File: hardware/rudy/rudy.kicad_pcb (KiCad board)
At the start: 2 copper layers, 15.7 x 67.1 mm, 23 parts, among them IC1 ATMEGA328-P, P1 CONN1, P2 CONN2, P3 SERPROG, P4 USB_B, U1 LD1117S33TR, Y1 Crystal

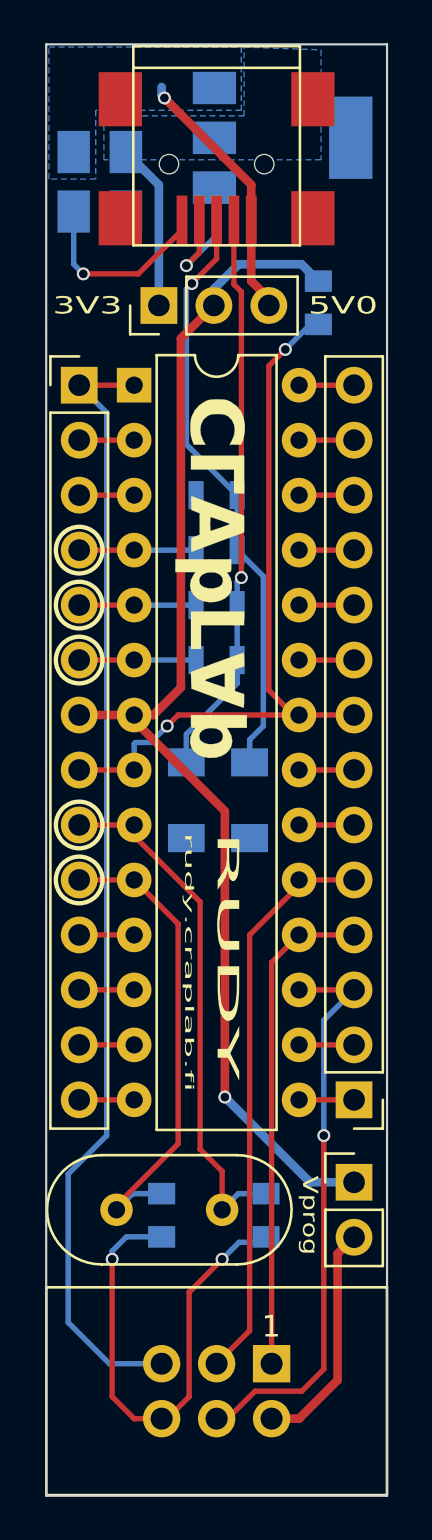
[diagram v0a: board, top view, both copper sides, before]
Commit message: Changed Zener diodes
Changed footprint for D1 and D2 Zener diodes from Mini MILF to SOD-323F
and moved their position in front of R1 and R2.

That came with a bit of rerouting, and trying to keep the pad position
close enough to the initial ones, so I don't have to order new stencils
right away (while even still waiting for them)
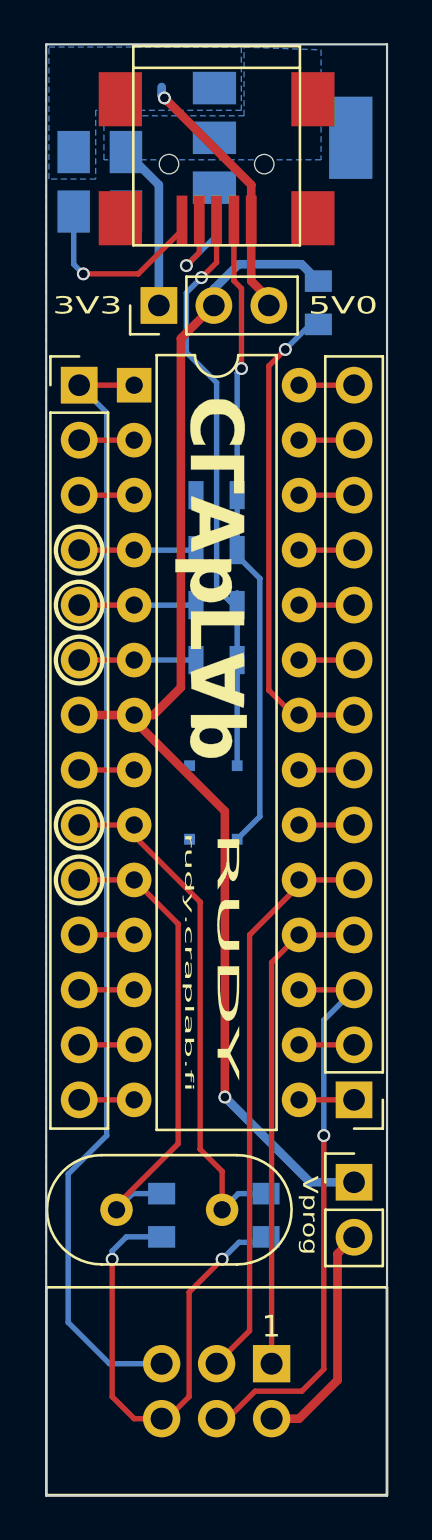
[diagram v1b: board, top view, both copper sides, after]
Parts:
- D1, D2: footprint Diodes_SMD:D_MiniMELF -> Diodes_SMD:D_SOD-323F
- moved D2 2.46 mm to (76.0, 92.1), turned to 180 degrees
- moved D1 2.03 mm to (76.0, 88.7), turned to 180 degrees
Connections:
- P4 pad 2: Net-(D1-Pad1) -> Net-(D2-Pad1)
- P4 pad 3: Net-(D2-Pad1) -> Net-(D1-Pad1)
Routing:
- net GND: track 74.8 -> 65.4 mm, vias 6 -> 5
- net Net-(D2-Pad1): track 27.4 -> 29.7 mm
- net Net-(D1-Pad1): track 26.8 -> 27.4 mm

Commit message: Fixed USB-B component after KiCad update
Turns out 1-3-2-4-5 is a more logical pin arrangement for some people,
and I fucked up paying attention to this, so D+ and D- USB lines got
swapped in the schematic component. Should have been more suspicious
why I had to do so much re-routing after updating the Zener diodes.
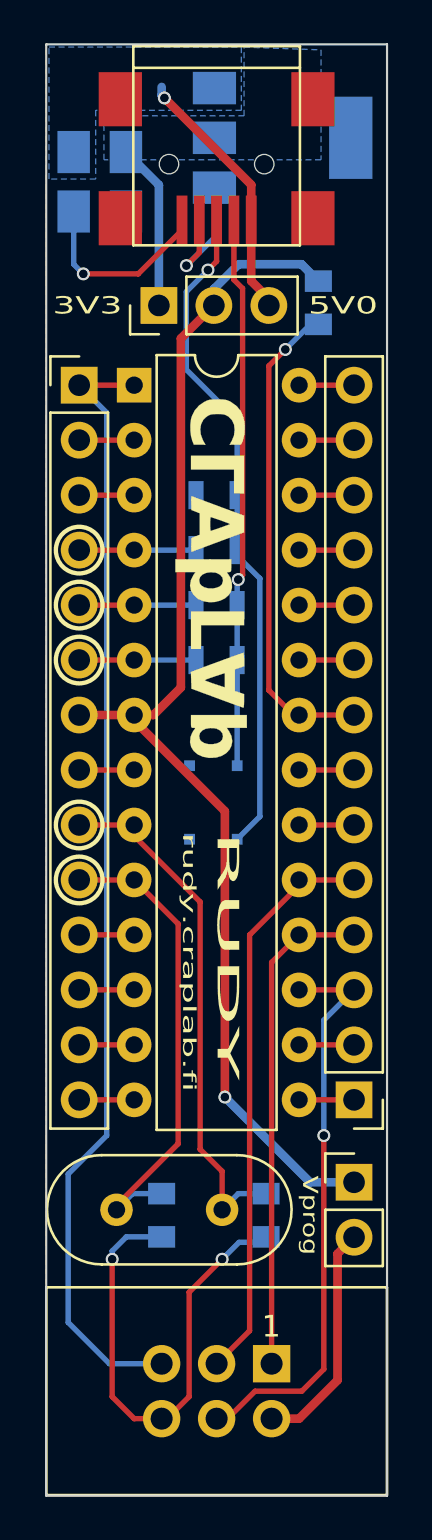
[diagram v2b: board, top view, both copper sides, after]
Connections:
- P4 pad 2: Net-(D2-Pad1) -> Net-(D1-Pad1)
- P4 pad 3: Net-(D1-Pad1) -> Net-(D2-Pad1)
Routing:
- net Net-(D2-Pad1): track 29.7 -> 31.0 mm
- net Net-(D1-Pad1): track 27.4 -> 26.2 mm

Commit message: HW: added LEDs and AVCC cap
There were no LEDs.
Why were there no LEDs?!
Everything needs LEDs!

So now there are, indicating that the device is actually powered, which
will lessen occasional confusion about that (especially when one forgets
to adjust the jumper after flashing).

But simple LED alone is boring, so there's now two below the IC itself,
giving a great glow to the device.

Note that this is really only just a power indication and not routed to
any output pin, so the LEDs are always on and can't be controlled by the
microcontroller itself -- at least at this point.

Also added 100nF cap to decouple VCC and AVCC, just in case.
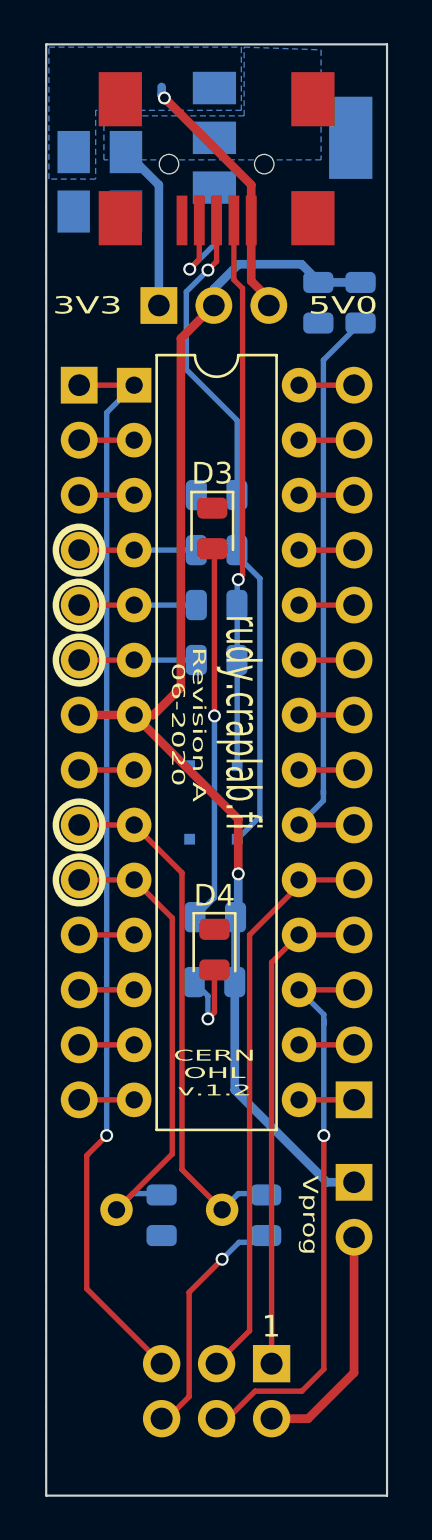
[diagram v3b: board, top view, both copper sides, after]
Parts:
- removed G***: LOGO, Artwork_4chord-midi:oshw_50
- removed G***: LOGO, Artwork_4chord-midi:craplab-2400
- removed G1: LOGO, Artwork_4chord-midi:craplab
- added C6: 100n, Capacitor_SMD:C_0805_2012Metric, B.Cu at (82.8, 67.3)
- added D3: LED, LED_SMD:LED_0805_2012Metric, F.Cu at (76.0, 77.7)
- added D4: LED, LED_SMD:LED_0805_2012Metric, F.Cu at (76.1, 97.2)
- added R5: 120R, Resistor_SMD:R_0805_2012Metric, B.Cu at (76.1, 95.7)
- added R6: 120R, Resistor_SMD:R_0805_2012Metric, B.Cu at (76.1, 98.7)
- added oshw: LOGO, Artwork_4chord-midi:oshw_50, B.Cu at (76.2, 103.5)
- C1, C4, C5: footprint Capacitors_SMD:C_0805 -> Capacitor_SMD:C_0805_2012Metric
- R1, R2, R3, R4: footprint Resistors_SMD:R_0805 -> Resistor_SMD:R_0805_2012Metric
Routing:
- net GND: track 65.3 -> 25.1 mm, vias 5 -> 2
- net /AVCC: track 2.54 -> 27.1 mm
- net Net-(D3-Pad2): track 0.00 -> 17.4 mm, vias 0 -> 1
- net Net-(D4-Pad2): track 0.00 -> 4.35 mm, vias 0 -> 1
- net /#RESET: track 52.7 -> 50.6 mm, vias 0 -> 1
- net /VCC: track 58.2 -> 59.6 mm
- net /PB6: track 25.1 -> 25.6 mm
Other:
- board text added: "Revision A 06-2020"
- board text removed: "Revision A 08-2017"
